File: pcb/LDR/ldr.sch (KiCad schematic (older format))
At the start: 6 parts, among them J1 RJ45

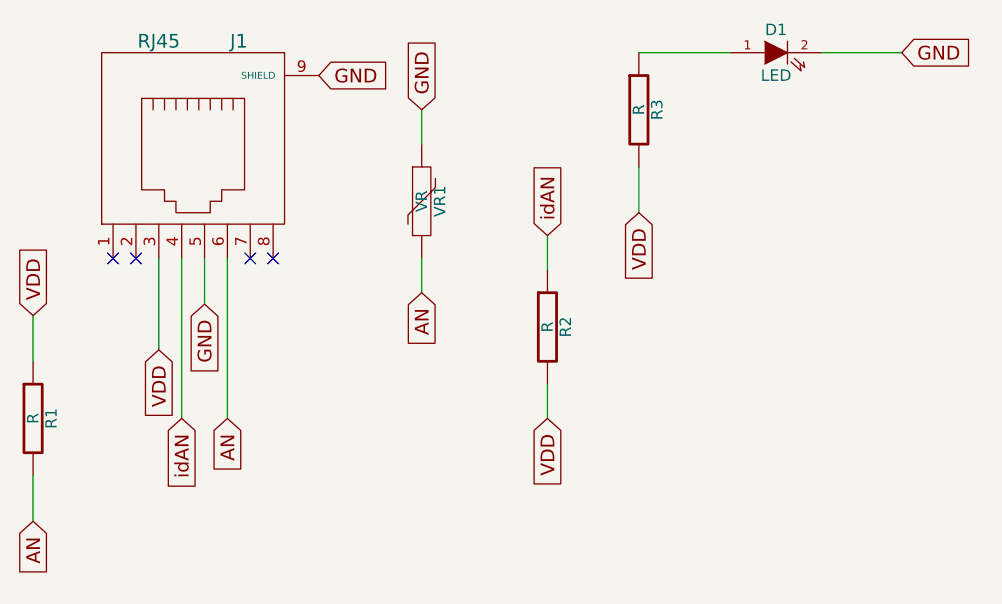
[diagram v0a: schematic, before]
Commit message: Set Resistance value in ldr sensor
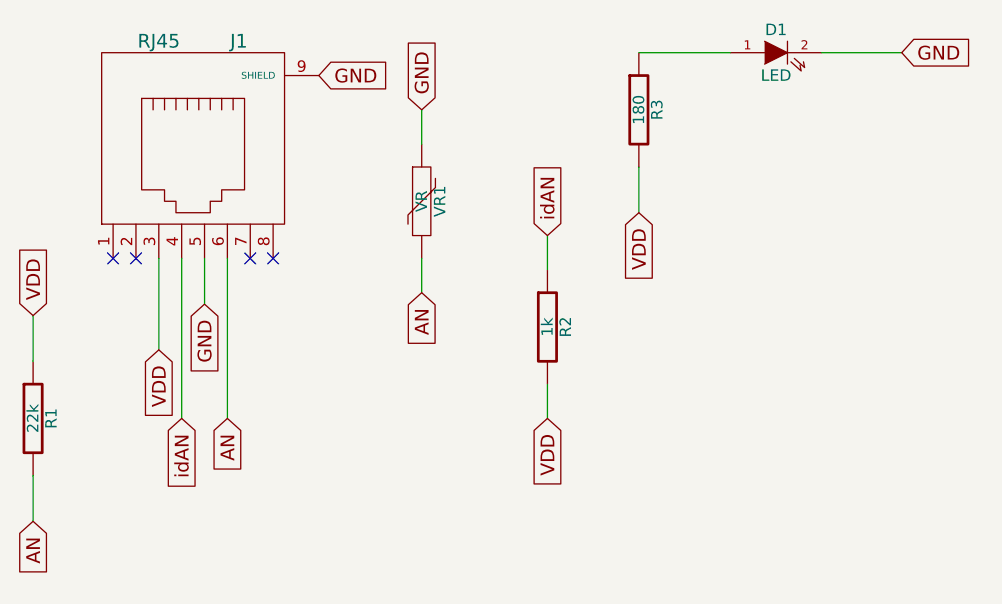
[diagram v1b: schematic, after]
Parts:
- R1: value R -> 22k
- R2: value R -> 1k
- R3: value R -> 180
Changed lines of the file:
@@
-EESchema Schematic File Version 2  date mar 15 may 2012 10:41:56 UYT
+EESchema Schematic File Version 2  date mié 23 may 2012 12:39:40 UYT
 LIBS:power
 LIBS:device
@@
 LIBS:contrib
 LIBS:valves
+LIBS:ldr-cache
 EELAYER 25  0
 EELAYER END
@@
 Sheet 1 1
 Title ""
-Date "15 may 2012"
+Date "23 may 2012"
 Rev ""
 Comp ""
@@
 P 4300 1300
 F 0 "R3" V 4380 1300 50  0000 C CNN
-F 1 "R" V 4300 1300 50  0000 C CNN
+F 1 "180" V 4300 1300 50  0000 C CNN
 	1    4300 1300
 	1    0    0    -1
@@
 P 3900 2250
 F 0 "R2" V 3980 2250 50  0000 C CNN
-F 1 "R" V 3900 2250 50  0000 C CNN
+F 1 "1k" V 3900 2250 50  0000 C CNN
 	1    3900 2250
 	1    0    0    -1
@@
 P 1650 2650
 F 0 "R1" V 1730 2650 50  0000 C CNN
-F 1 "R" V 1650 2650 50  0000 C CNN
+F 1 "22k" V 1650 2650 50  0000 C CNN
 	1    1650 2650
 	1    0    0    -1
